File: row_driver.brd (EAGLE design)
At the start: 65 x 56 mm, 47 parts, among them IC1 MCP23017SO, Q1 BUK98150-55A, Q2 BUK98150-55A, Q3 BUK98150-55A, Q4 BUK98150-55A, Q5 BUK98150-55A, Q6 BUK98150-55A, Q7 BUK98150-55A, Q8 BUK98150-55A, Q9 BUK98150-55A

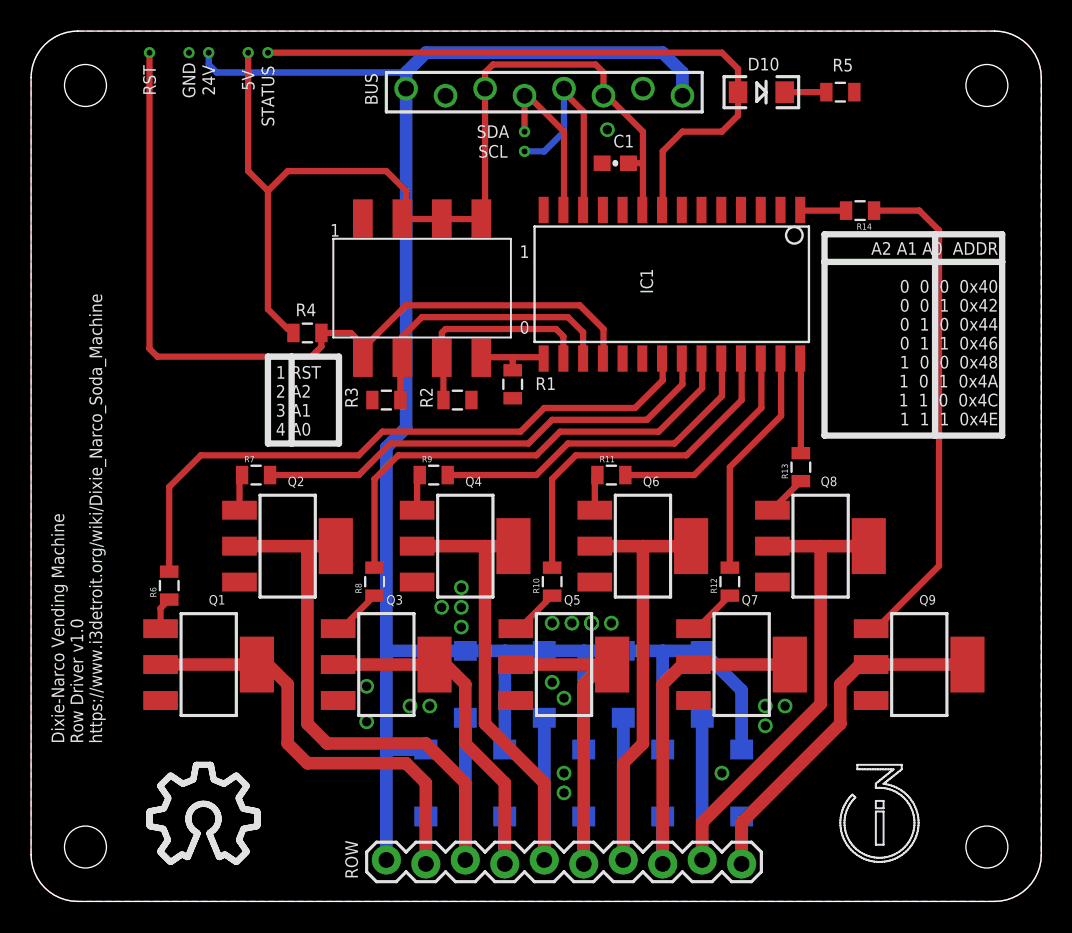
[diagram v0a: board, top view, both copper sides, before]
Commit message: Added relay header for the ubiquitous 4-channel relay boards. Two are immediately assigned: one acts in NC in series with the compressor (so the controller can interrupt compressor power on demand, but failures restore compressor power); the other acts in NO in parallel with the bimetal thermostat (so the controller can short across it and have full compressor control, but failures allow it to function)
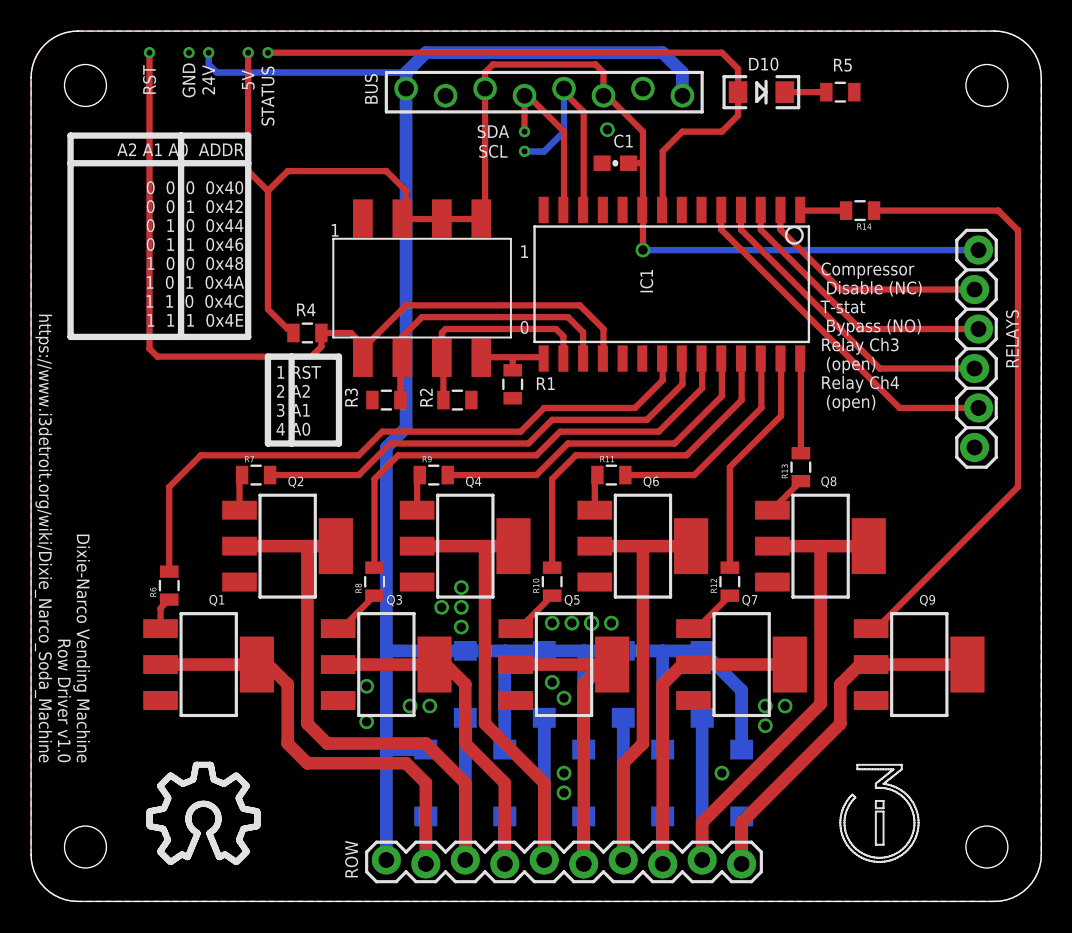
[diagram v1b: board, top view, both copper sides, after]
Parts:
- added RELAYS: (no value), SparkFun-Connectors:1X06_LOCK
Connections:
- new net COMP_DISABLE: IC1.2, RELAYS.2
- new net RLY_CH3: IC1.4, RELAYS.4
- new net RLY_CH4: IC1.5, RELAYS.5
- new net TSTAT_BYPASS: IC1.3, RELAYS.3
- net +5V: now also RELAYS.1
- net GND: now also RELAYS.6
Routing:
- net +5V: track 64.8 -> 89.0 mm, vias 0 -> 1
- net RLY_CH4: track 0.00 -> 22.6 mm
- net RLY_CH3: track 0.00 -> 20.0 mm
- net TSTAT_BYPASS: track 0.00 -> 17.9 mm
- net COMP_DISABLE: track 0.00 -> 15.4 mm
- net ROW_S_8: track 32.3 -> 39.5 mm
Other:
- board text added: "Compressor Disable (NC) T-stat Bypass (NO) Relay Ch3 (open) Relay Ch4 (open)"
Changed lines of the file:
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@@
 <hole x="61.5" y="52.5" drill="2.7"/>
 <hole x="61.5" y="3.5" drill="2.7"/>
-<text x="62.23" y="42.418" size="0.8128" layer="25" rot="R180">A2 A1 A0  ADDR
+<text x="13.716" y="48.768" size="0.8128" layer="25" rot="R180">A2 A1 A0  ADDR
  0  0  0  0x40
  0  0  1  0x42
@@
  1  1  0  0x4C
  1  1  1  0x4E</text>
-<wire x1="51.054" y1="42.926" x2="58.166" y2="42.926" width="0.4064" layer="25"/>
-<wire x1="58.166" y1="42.926" x2="62.484" y2="42.926" width="0.4064" layer="25"/>
-<wire x1="62.484" y1="42.926" x2="62.484" y2="41.148" width="0.4064" layer="25"/>
-<wire x1="62.484" y1="41.148" x2="62.484" y2="29.972" width="0.4064" layer="25"/>
-<wire x1="62.484" y1="29.972" x2="58.166" y2="29.972" width="0.4064" layer="25"/>
-<wire x1="58.166" y1="29.972" x2="51.054" y2="29.972" width="0.4064" layer="25"/>
-<wire x1="51.054" y1="29.972" x2="51.054" y2="41.148" width="0.4064" layer="25"/>
-<wire x1="51.054" y1="41.148" x2="51.054" y2="42.926" width="0.4064" layer="25"/>
-<wire x1="51.054" y1="41.148" x2="62.484" y2="41.148" width="0.4064" layer="25"/>
-<wire x1="58.166" y1="42.926" x2="58.166" y2="29.972" width="0.4064" layer="25"/>
+<wire x1="2.54" y1="49.276" x2="9.652" y2="49.276" width="0.4064" layer="25"/>
+<wire x1="9.652" y1="49.276" x2="13.97" y2="49.276" width="0.4064" layer="25"/>
+<wire x1="13.97" y1="49.276" x2="13.97" y2="47.498" width="0.4064" layer="25"/>
+<wire x1="13.97" y1="47.498" x2="13.97" y2="36.322" width="0.4064" layer="25"/>
+<wire x1="13.97" y1="36.322" x2="9.652" y2="36.322" width="0.4064" layer="25"/>
+<wire x1="9.652" y1="36.322" x2="2.54" y2="36.322" width="0.4064" layer="25"/>
+<wire x1="2.54" y1="36.322" x2="2.54" y2="47.498" width="0.4064" layer="25"/>
+<wire x1="2.54" y1="47.498" x2="2.54" y2="49.276" width="0.4064" layer="25"/>
+<wire x1="2.54" y1="47.498" x2="13.97" y2="47.498" width="0.4064" layer="25"/>
+<wire x1="9.652" y1="49.276" x2="9.652" y2="36.322" width="0.4064" layer="25"/>
 <text x="15.748" y="29.972" size="0.8128" layer="25">1 RST
 2 A2
@@
 <wire x1="16.764" y1="29.464" x2="15.24" y2="29.464" width="0.4064" layer="25"/>
 <wire x1="16.764" y1="35.052" x2="16.764" y2="29.464" width="0.4064" layer="25"/>
-<text x="4.572" y="10.16" size="0.8128" layer="25" rot="R90">Dixie-Narco Vending Machine
+<text x="0.508" y="8.89" size="0.8128" layer="25" rot="SR270" align="bottom-right">Dixie-Narco Vending Machine
 Row Driver v1.0
 https://www.i3detroit.org/wiki/Dixie_Narco_Soda_Machine</text>
@@
 <text x="31.75" y="39.37" size="0.8128" layer="25" align="center">1
 0</text>
+<text x="50.8" y="31.75" size="0.8128" layer="25">Compressor
+ Disable (NC)
+T-stat
+ Bypass (NO)
+Relay Ch3
+ (open)
+Relay Ch4
+ (open)</text>
 </plain>
 <attributes>
@@
 <element name="R13" library="SparkFun-Passives" package="0805" value="220" x="49.53" y="27.94" rot="R90"/>
 <element name="R14" library="SparkFun-Passives" package="0805" value="220" x="53.34" y="44.45" rot="R180"/>
+<element name="RELAYS" library="SparkFun-Connectors" package="1X06_LOCK" value="" x="60.96" y="41.91" smashed="yes" rot="R270">
+<attribute name="NAME" x="62.738" y="38.1" size="0.8128" layer="25" font="vector" rot="R270"/>
+<attribute name="VALUE" x="57.658" y="43.18" size="1.27" layer="27" font="vector" rot="R270"/>
+</element>
 </elements>
 <signals>
@@
 <via x="21.59" y="11.557" extent="1-16" drill="0.6"/>
 <via x="21.59" y="13.843" extent="1-16" drill="0.6"/>
+<contactref element="RELAYS" pad="6"/>
 </signal>
 <signal name="I2C1_SCL">
@@
 <wire x1="40.64" y1="48.26" x2="40.64" y2="44.53" width="0.4064" layer="1"/>
 <wire x1="40.64" y1="44.53" x2="40.6" y2="44.49" width="0.4064" layer="1"/>
-<contactref element="STATUS" pad="P$1"/>
 <contactref element="STATUS" pad="P$1"/>
 <wire x1="15.24" y1="54.61" x2="44.45" y2="54.61" width="0.4064" layer="1"/>
@@
 <wire x1="13.97" y1="46.99" x2="15.24" y2="45.72" width="0.4064" layer="1"/>
 <wire x1="38.442" y1="47.498" x2="39.37" y2="47.498" width="0.4064" layer="1"/>
+<contactref element="RELAYS" pad="1"/>
+<wire x1="60.96" y1="41.91" x2="39.37" y2="41.91" width="0.4064" layer="16"/>
+<via x="39.37" y="41.91" extent="1-16" drill="0.6"/>
+<wire x1="39.37" y1="41.91" x2="39.37" y2="44.45" width="0.4064" layer="1"/>
+<wire x1="39.37" y1="44.45" x2="39.33" y2="44.49" width="0.4064" layer="1"/>
 </signal>
 <signal name="+24V">
@@
 <contactref element="R14" pad="1"/>
 <wire x1="54.0512" y1="17.5514" x2="54.3814" y2="17.5514" width="0.4064" layer="1"/>
-<wire x1="54.3814" y1="17.5514" x2="58.42" y2="21.59" width="0.4064" layer="1"/>
-<wire x1="58.42" y1="21.59" x2="58.42" y2="43.18" width="0.4064" layer="1"/>
-<wire x1="58.42" y1="43.18" x2="57.15" y2="44.45" width="0.4064" layer="1"/>
-<wire x1="57.15" y1="44.45" x2="54.24" y2="44.45" width="0.4064" layer="1"/>
+<wire x1="54.3814" y1="17.5514" x2="63.5" y2="26.67" width="0.4064" layer="1"/>
+<wire x1="63.5" y1="26.67" x2="63.5" y2="43.18" width="0.4064" layer="1"/>
+<wire x1="63.5" y1="43.18" x2="62.23" y2="44.45" width="0.4064" layer="1"/>
+<wire x1="62.23" y1="44.45" x2="54.24" y2="44.45" width="0.4064" layer="1"/>
+</signal>
+<signal name="COMP_DISABLE">
+<contactref element="IC1" pad="2"/>
+<contactref element="RELAYS" pad="2"/>
+<wire x1="48.22" y1="44.49" x2="48.22" y2="43.22" width="0.4064" layer="1"/>
+<wire x1="48.22" y1="43.22" x2="52.07" y2="39.37" width="0.4064" layer="1"/>
+<wire x1="52.07" y1="39.37" x2="60.706" y2="39.37" width="0.4064" layer="1"/>
+</signal>
+<signal name="TSTAT_BYPASS">
+<contactref element="IC1" pad="3"/>
+<contactref element="RELAYS" pad="3"/>
+<wire x1="46.95" y1="44.49" x2="46.95" y2="43.22" width="0.4064" layer="1"/>
+<wire x1="46.95" y1="43.22" x2="53.34" y2="36.83" width="0.4064" layer="1"/>
+<wire x1="53.34" y1="36.83" x2="60.96" y2="36.83" width="0.4064" layer="1"/>
+</signal>
+<signal name="RLY_CH3">
+<contactref element="IC1" pad="4"/>
+<contactref element="RELAYS" pad="4"/>
+<wire x1="45.68" y1="44.49" x2="45.68" y2="43.22" width="0.4064" layer="1"/>
+<wire x1="45.68" y1="43.22" x2="54.61" y2="34.29" width="0.4064" layer="1"/>
+<wire x1="54.61" y1="34.29" x2="60.706" y2="34.29" width="0.4064" layer="1"/>
+</signal>
+<signal name="RLY_CH4">
+<contactref element="IC1" pad="5"/>
+<contactref element="RELAYS" pad="5"/>
+<wire x1="44.41" y1="44.49" x2="44.41" y2="43.22" width="0.4064" layer="1"/>
+<wire x1="44.41" y1="43.22" x2="55.88" y2="31.75" width="0.4064" layer="1"/>
+<wire x1="55.88" y1="31.75" x2="60.96" y2="31.75" width="0.4064" layer="1"/>
 </signal>
 </signals>
